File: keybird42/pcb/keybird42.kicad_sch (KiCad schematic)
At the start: 174 parts, among them J1 IObird FPC, SW111 SW_MX, SW112 SW_MX, SW113 SW_MX, SW114 SW_MX, SW115 SW_MX, SW116 SW_MX, SW117 SW_MX, SW121 SW_MX, SW122 SW_MX, SW123 SW_MX, SW124 SW_MX, SW125 SW_MX, SW126 SW_MX, SW127 SW_MX, SW131 SW_MX, SW132 SW_MX, SW133 SW_MX, SW134 SW_MX, SW135 SW_MX, SW136 SW_MX, SW137 SW_MX, SW211 SW_MX, SW212 SW_MX, SW213 SW_MX, SW214 SW_MX, SW215 SW_MX, SW216 SW_MX, SW217 SW_MX, SW221 SW_MX, SW222 SW_MX, SW223 SW_MX, SW225 SW_MX, SW226 SW_MX, SW227 SW_MX, SW231 SW_MX, SW232 SW_MX, SW233 SW_MX, SW234 SW_MX, SW235 SW_MX, SW236 SW_MX, SW237 SW_MX, SW311 SW_MX, SW312 SW_MX, SW314 SW_MX, SW315 SW_MX, SW316 SW_MX, SW317 SW_MX, SW321 SW_MX, SW322 SW_MX, SW323 SW_MX, SW324 SW_MX, SW325 SW_MX, SW327 SW_MX, SW331 SW_MX, SW332 SW_MX, SW333 SW_MX, SW334 SW_MX, SW335 SW_MX, SW336 SW_MX, SW337 SW_MX, SW411 SW_MX, SW412 SW_MX, SW413 SW_MX, SW414 SW_MX, SW415 SW_MX, SW416 SW_MX, SW417 SW_MX, SW421 SW_MX, SW423 SW_MX, SW424 SW_MX, SW425 SW_MX, SW426 SW_MX, SW427 SW_MX, SW431 SW_MX, SW432 SW_MX, SW433 SW_MX, SW434 SW_MX, SW436 SW_MX, SW437 SW_MX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

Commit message: done?
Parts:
- SW111: value SW_MX -> F1
- SW112: value SW_MX -> ESC
- SW113: value SW_MX -> 3#
- SW114: value SW_MX -> 6^
- SW115: value SW_MX -> 9(
- SW116: value SW_MX -> PLUS
- SW117: value SW_MX -> F13
- SW121: value SW_MX -> F5
- SW122: value SW_MX -> 1!
- SW123: value SW_MX -> 4$
- SW124: value SW_MX -> 7&
- SW125: value SW_MX -> 0)
- SW126: value SW_MX -> LSLASH
- SW127: value SW_MX -> F14
- SW131: value SW_MX -> F9
- SW132: value SW_MX -> 2@
- SW133: value SW_MX -> 5%
- SW134: value SW_MX -> 8*
- SW135: value SW_MX -> MINUS
- SW136: value SW_MX -> LQUOTE
- SW137: value SW_MX -> F15
- SW211: value SW_MX -> F2
- SW212: value SW_MX -> TAB
- SW213: value SW_MX -> E
- SW214: value SW_MX -> Y
- SW215: value SW_MX -> I
- SW216: value SW_MX -> [{
- SW217: value SW_MX -> F16
- SW221: value SW_MX -> F6
- SW222: value SW_MX -> Q
- SW223: value SW_MX -> R
- SW225: value SW_MX -> O
- SW226: value SW_MX -> ]}
- SW227: value SW_MX -> F17
- SW231: value SW_MX -> F10
- SW232: value SW_MX -> W
- SW233: value SW_MX -> T
- SW234: value SW_MX -> U
- SW235: value SW_MX -> P
- SW236: value SW_MX -> DELETE
- SW237: value SW_MX -> F18
- SW311: value SW_MX -> F3
- SW312: value SW_MX -> LCTRL
- SW314: value SW_MX -> G
- SW315: value SW_MX -> K
- SW316: value SW_MX -> RQUOTE
- SW317: value SW_MX -> F19
- SW321: value SW_MX -> F7
- SW322: value SW_MX -> A
- SW323: value SW_MX -> D
- SW324: value SW_MX -> H
- SW325: value SW_MX -> L
- SW327: value SW_MX -> UP
- SW331: value SW_MX -> F11
- SW332: value SW_MX -> S
- SW333: value SW_MX -> F
- SW334: value SW_MX -> J
- SW335: value SW_MX -> COLON
- SW336: value SW_MX -> RETURN
- SW337: value SW_MX -> F20
- SW411: value SW_MX -> F4
- SW412: value SW_MX -> LSHIFT
- SW413: value SW_MX -> X
- SW414: value SW_MX -> B
- SW415: value SW_MX -> COMMA
- SW416: value SW_MX -> RSLASH
- SW417: value SW_MX -> LEFT
- SW421: value SW_MX -> F8
- SW423: value SW_MX -> C
- SW424: value SW_MX -> N
- SW425: value SW_MX -> DOT
- SW426: value SW_MX -> RSHIFT
- SW427: value SW_MX -> DOWN
- SW431: value SW_MX -> F12
- SW432: value SW_MX -> Z
- SW433: value SW_MX -> V
- SW434: value SW_MX -> M
- SW436: value SW_MX -> RFUN
- SW437: value SW_MX -> RIGHT
- SW501: value SW_MX -> LFUN
- SW502: value SW_MX -> LALT
- SW503: value SW_MX -> LMETA
- SW504: value SW_MX -> SPACE
- SW505: value SW_MX -> RMETA
- SW506: value SW_MX -> RALT
- SW507: value SW_MX -> RCTRL

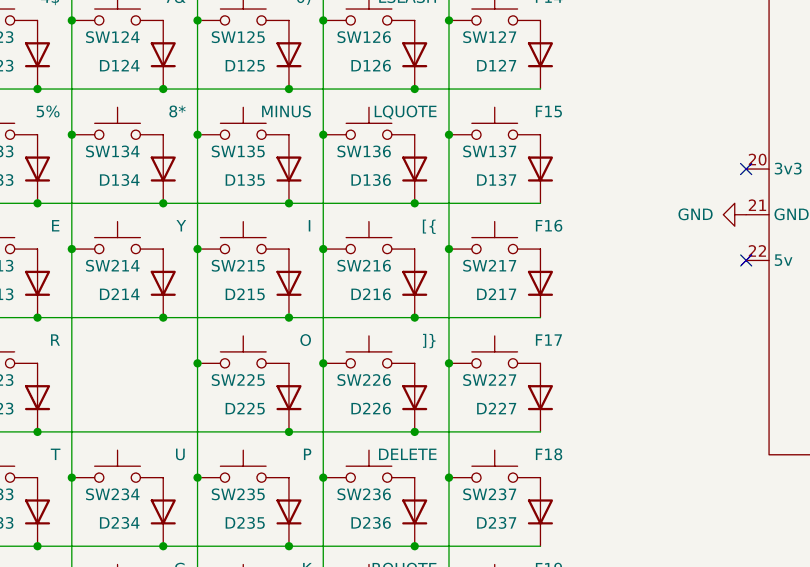
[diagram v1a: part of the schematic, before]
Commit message: better names for bracket keys
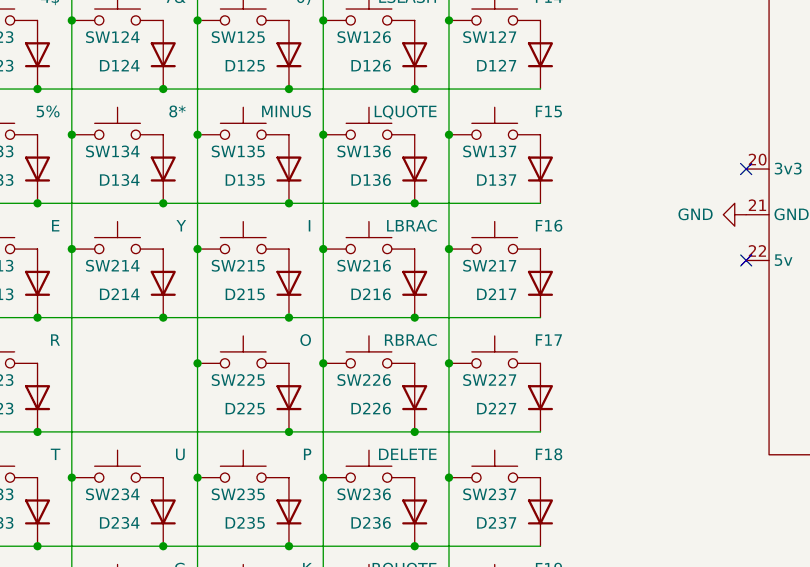
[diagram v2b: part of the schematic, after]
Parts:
- SW216: value [{ -> LBRAC
- SW226: value ]} -> RBRAC
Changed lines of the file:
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@@
       (effects (font (size 1.27 1.27)) (justify right))
     )
-    (property "Value" "]}" (at 115.57 66.04 0)
+    (property "Value" "RBRAC" (at 115.57 66.04 0)
       (effects (font (size 1.27 1.27)) (justify right))
     )
@@
       (effects (font (size 1.27 1.27)) (justify right))
     )
-    (property "Value" "[{" (at 115.57 53.34 0)
-      (effects (font (size 1.27 1.27)) (justify right))
-    )
+    (property "Value" "LBRAC" (at 115.57 53.34 0)
+      (effects (font (size 1.27 1.27)) (justify right))
+    )

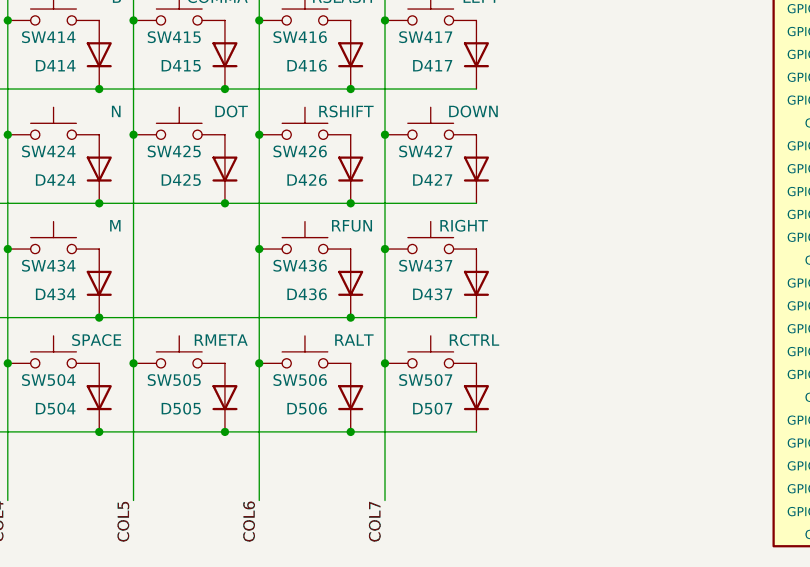
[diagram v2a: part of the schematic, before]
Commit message: include keycap outlines and stabilizers in switch footprints
so far only updated the schematic, pcb next
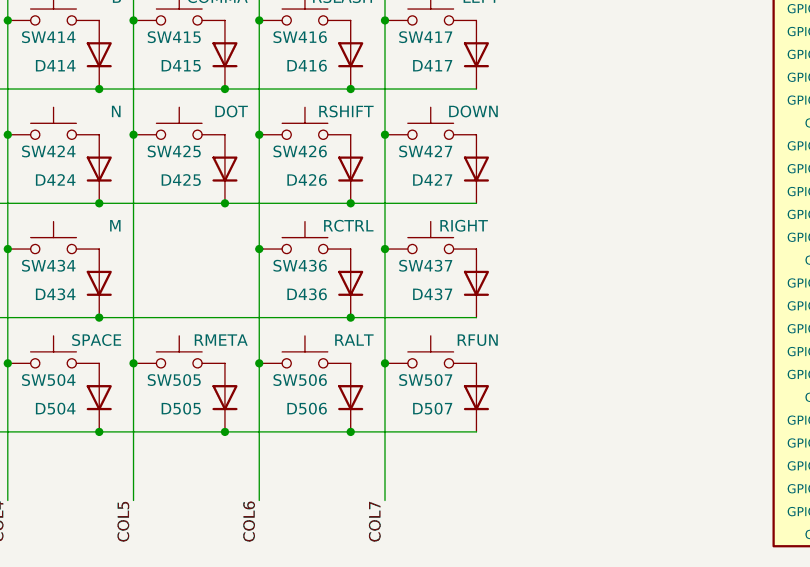
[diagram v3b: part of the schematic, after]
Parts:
- SW111, SW112, SW113, SW114, SW115, SW116, SW117, SW121, SW122, SW123, SW124, SW125, SW126, SW127, SW131, SW132, SW133, SW134, SW135, SW136, SW137, SW211, SW213, SW214, SW215, SW216, SW217, SW221, SW222, SW223, SW225, SW226, SW227, SW231, SW232, SW233, SW234, SW235, SW237, SW311, SW314, SW315, SW316, SW317, SW321, SW322, SW323, SW324, SW325, SW327, SW331, SW332, SW333, SW334, SW335, SW337, SW411, SW413, SW414, SW415, SW416, SW417, SW421, SW423, SW424, SW425, SW427, SW431, SW432, SW433, SW434, SW437: symbol keybird42:SW_MX -> keybird42:SW_MX_1.00u
- SW212, SW236, SW503, SW505: footprint keybird42:SW_Hotswap_Kailh_MX -> keybird42:SW_Hotswap_Kailh_MX_1.50u; symbol keybird42:SW_MX -> keybird42:SW_MX_1.50u
- SW312, SW426: footprint keybird42:SW_Hotswap_Kailh_MX -> keybird42:SW_Hotswap_Kailh_MX_1.75u; symbol keybird42:SW_MX -> keybird42:SW_MX_1.75u
- SW336, SW412: footprint keybird42:SW_Hotswap_Kailh_MX -> keybird42:SW_Hotswap_Kailh_MX_2.25u; symbol keybird42:SW_MX -> keybird42:SW_MX_2.25u
- SW436: value RFUN -> RCTRL; footprint keybird42:SW_Hotswap_Kailh_MX -> keybird42:SW_Hotswap_Kailh_MX_1.00u; symbol keybird42:SW_MX -> keybird42:SW_MX_1.00u
- SW501, SW502, SW506: footprint keybird42:SW_Hotswap_Kailh_MX -> keybird42:SW_Hotswap_Kailh_MX_1.25u; symbol keybird42:SW_MX -> keybird42:SW_MX_1.25u
- SW504: footprint keybird42:SW_Hotswap_Kailh_MX -> keybird42:SW_Hotswap_Kailh_MX_7.00u; symbol keybird42:SW_MX -> keybird42:SW_MX_7.00u
- SW507: value RCTRL -> RFUN; footprint keybird42:SW_Hotswap_Kailh_MX -> keybird42:SW_Hotswap_Kailh_MX_1.25u; symbol keybird42:SW_MX -> keybird42:SW_MX_1.25u
